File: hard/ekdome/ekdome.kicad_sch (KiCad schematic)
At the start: 96 parts, among them J10 USB_P, J11 DBG, J20 HBS, J21 HBS, J30 POWER, Q20 NP, Q21 NP, U10 CH32V203C8T6, U11 CH340E, U13 74LVC1G86, U20 MS1192, U30 XL1509, U31 AMS1117-3.3, Y10 12M

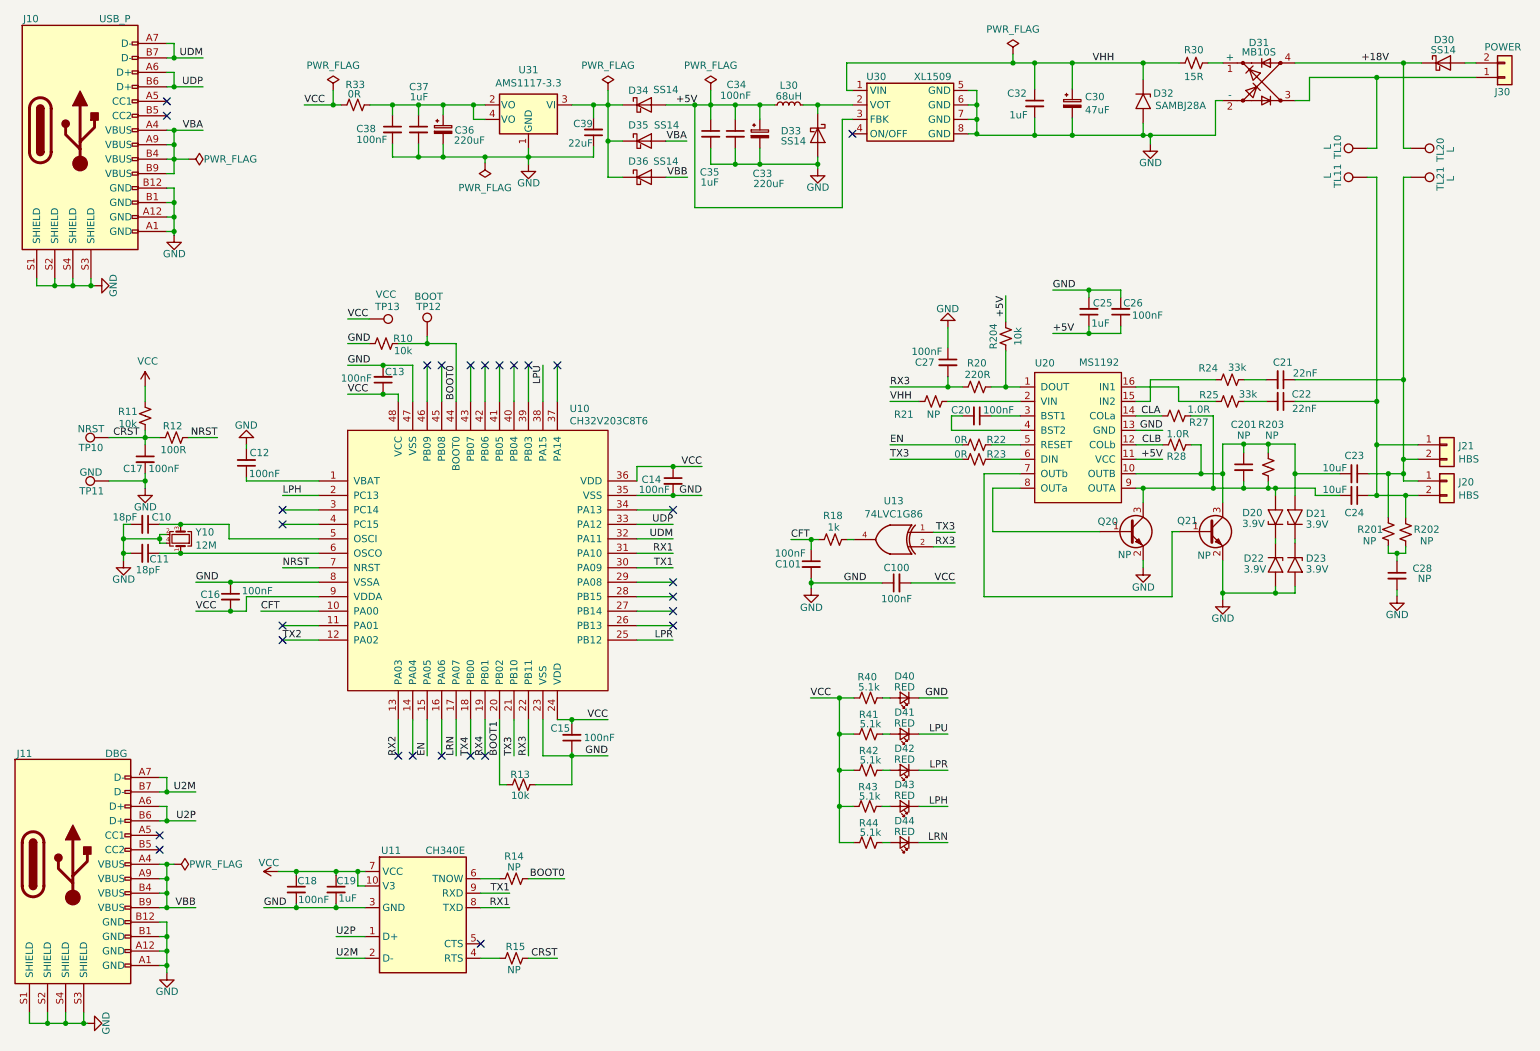
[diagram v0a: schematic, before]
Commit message: 增加485端口用于协议调试
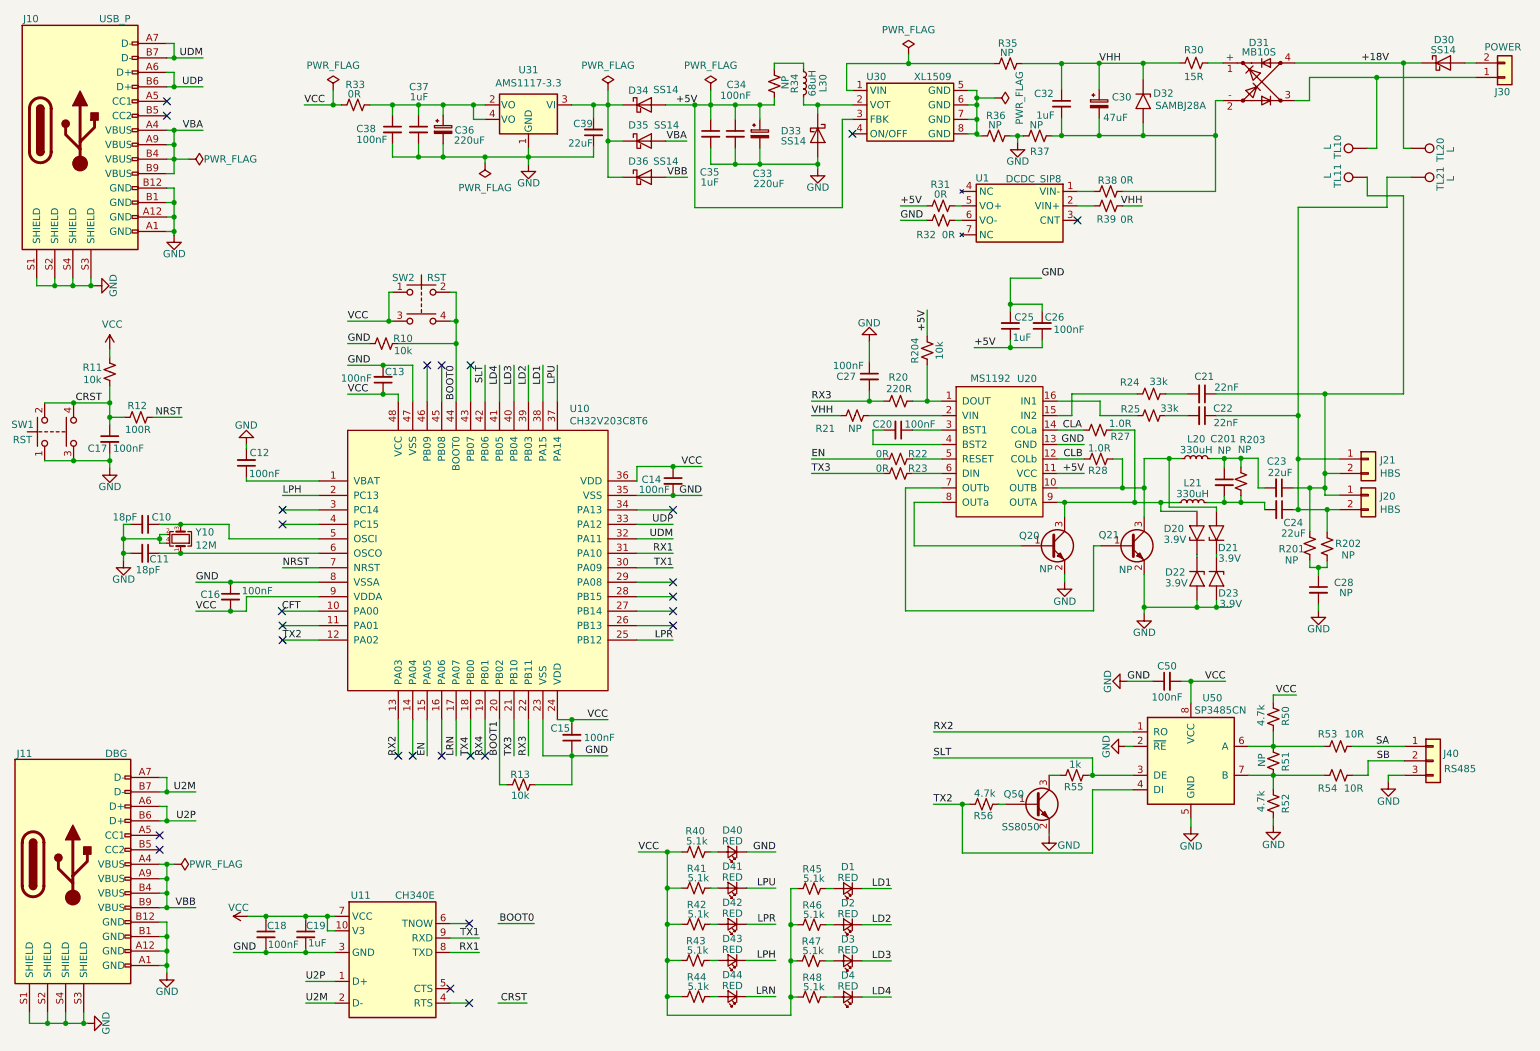
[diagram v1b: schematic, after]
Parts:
- removed C101: 100nF, kicad_footpring_general:C_0603_1608Metric, symbol kicad_symbol_general:C_Small
- removed R14, R15: NP, kicad_footprint_general:R_0603_1608Metric, symbol kicad_symbol_general:R_Small_US
- removed R18: 1k, kicad_footpring_general:R_0603_1608Metric, symbol kicad_symbol_general:R_Small_US
- removed TP10: NRST, kicad_footprint_general:TestPoint_THTPad_D1.0mm_Drill0.5mm, symbol Connector:TestPoint
- removed TP11: GND, kicad_footprint_general:TestPoint_THTPad_D1.0mm_Drill0.5mm, symbol Connector:TestPoint
- removed TP12: BOOT, kicad_footprint_general:TestPoint_THTPad_D1.0mm_Drill0.5mm, symbol Connector:TestPoint
- removed TP13: VCC, kicad_footprint_general:TestPoint_THTPad_D1.0mm_Drill0.5mm, symbol Connector:TestPoint
- removed U13: 74LVC1G86, kicad_footpring_general:SOT-23-5, symbol kicad_symbol_general_s:74LVC1G86
- added D1, D2, D3, D4: RED, kicad_footprint_general:LED_0603_1608Metric, symbol kicad_symbol_general:LED_Small
- added J40: RS485, kicad_footprint_general:PhoenixContact_MCV_1,5_3-G-3.81_1x03_P3.81mm_Vertical, symbol kicad_symbol_general_s:Conn_01x03
- added L20, L21: 330uH, Inductor_SMD:L_Bourns-SRN4018, symbol kicad_symbol_general:L_Small
- added Q50: SS8050, kicad_footprint_general:SOT-23, symbol kicad_symbol_general:Q_NPN_BEC
- added R31, R32, R38, R39: 0R, kicad_footprint_general:R_0805_2012Metric, symbol kicad_symbol_general:R_Small_US
- added R34, R35, R36, R37: NP, kicad_footprint_general:R_0805_2012Metric, symbol kicad_symbol_general:R_Small_US
- added R45, R46, R47, R48: 5.1k, kicad_footprint_general:R_0603_1608Metric, symbol kicad_symbol_general:R_Small_US
- added R50, R52, R56: 4.7k, kicad_footprint_general:R_0603_1608Metric, symbol kicad_symbol_general:R_Small_US
- added R51: NP, kicad_footprint_general:R_0603_1608Metric, symbol kicad_symbol_general:R_Small_US
- added R53, R54: 10R, kicad_footprint_general:R_1206_3216Metric, symbol kicad_symbol_general:R_Small_US
- added R55: 1k, kicad_footprint_general:R_0603_1608Metric, symbol kicad_symbol_general:R_Small_US
- added SW1, SW2: RST, kicad_footprint_general:SW_KAN0541, symbol kicad_symbol_general_s:SW_Push_Dual
- added U1: DCDC_SIP8, kicad_footprint_general:TDKSIP8, symbol kicad_symbol_general_s:DCDC_SIP8
- added U50: SP3485CN, kicad_footprint_general:SOIC-8_3.9x4.9mm_P1.27mm, symbol kicad_symbol_general_s:SP3485CN
- C23, C24: value 10uF -> 22uF; footprint kicad_footprint_general:C_1206_3216Metric -> kicad_footprint_general:CP_Elec_6.3x5.4
- renumbered C100 to C50
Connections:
- net +5V: now also R31.1, R34.2; no longer L30.1
- net BOOT0: now also SW2.2, SW2.4
- net CRST: now also SW1.2, SW1.4
- net GND: now also J40.3 (Pin_3), Q50.2 (E), R32.1, R36.2, R37.1, R52.2, SW1.1, SW1.3, U50.2 (~{RE}), U50.5 (GND); no longer C30.2, C32.2, D31.2 (-), D32.2 (A2), U30.5 (GND), U30.6 (GND), U30.7 (GND), U30.8 (GND)
- net LPU: now also U10.37 (PA14); no longer U10.38 (PA15)
- net RX2: now also U50.1 (RO)
- net TX2: now also R56.2, U50.4 (DI)
- net VCC: now also R45.1, R46.1, R47.1, R48.1, R50.1, SW2.1, SW2.3, U50.8 (VCC)
- net VHH: now also R35.2, R39.2; no longer U30.1 (VIN)
- net at D21.2 (A2), Q21.3 (C), R28.1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: now also L20.1; no longer C201.1, C23.2, R203.1
- net at D20.2 (A2), Q20.3 (C), R27.1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: now also L21.1; no longer C201.2, C24.2, R203.2
- net at C21.1, C23.1, J20.1 (Pin_1)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: now also TL11.1; no longer TL21.1
- net at C22.1, C24.1, J20.2 (Pin_2)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: now also TL21.1; no longer TL11.1
- net LD2: now reaches U10.39 (PB03)
- net LD2: now also D2.1 (K)
- net LD3: now reaches U10.40 (PB04)
- net LD3: now also D3.1 (K)
- net LD4: now reaches U10.41 (PB05)
- net LD4: now also D4.1 (K)
- net SLT: now reaches U10.42 (PB06)
- net SLT: now also R55.1, U50.3 (DE)
- new net: C201.1, C23.2, L20.2, R203.1
- new net: C201.2, C24.2, L21.2, R203.2
- new net: C30.2, C32.2, D31.2 (-), D32.2 (A2), R37.2, R38.2
- new net: R35.1, U30.1 (VIN)
- new net: R36.1, U30.5 (GND), U30.6 (GND), U30.7 (GND), U30.8 (GND)
- new net: L30.1, R34.1
- new net: D3.2 (A), R47.2
- new net: D2.2 (A), R46.2
- new net: R50.2, R51.1, R53.1, U50.6 (A)
- new net: Q50.3 (C), R55.2
- new net: R51.2, R52.1, R54.1, U50.7 (B)
- new net: R31.2, U1.5 (VO+)
- new net: D1.2 (A), R45.2
- new net: R39.1, U1.2 (VIN+)
- new net: D4.2 (A), R48.2
- new net: R38.1, U1.1 (VIN-)
- new net: R32.2, U1.6 (VO-)
- new net: Q50.1 (B), R56.1
- new net LD1: D1.1 (K), U10.38 (PA15)
- new net SA: J40.1 (Pin_1), R53.2
- new net SB: J40.2 (Pin_2), R54.2
- no-connect marks 28 -> 27
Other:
- moved on the sheet: C17, C18, C19, C20, C201, C21, C22, C23, C24, C25, C26, C27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
